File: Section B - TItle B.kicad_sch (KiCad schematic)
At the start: 0 parts

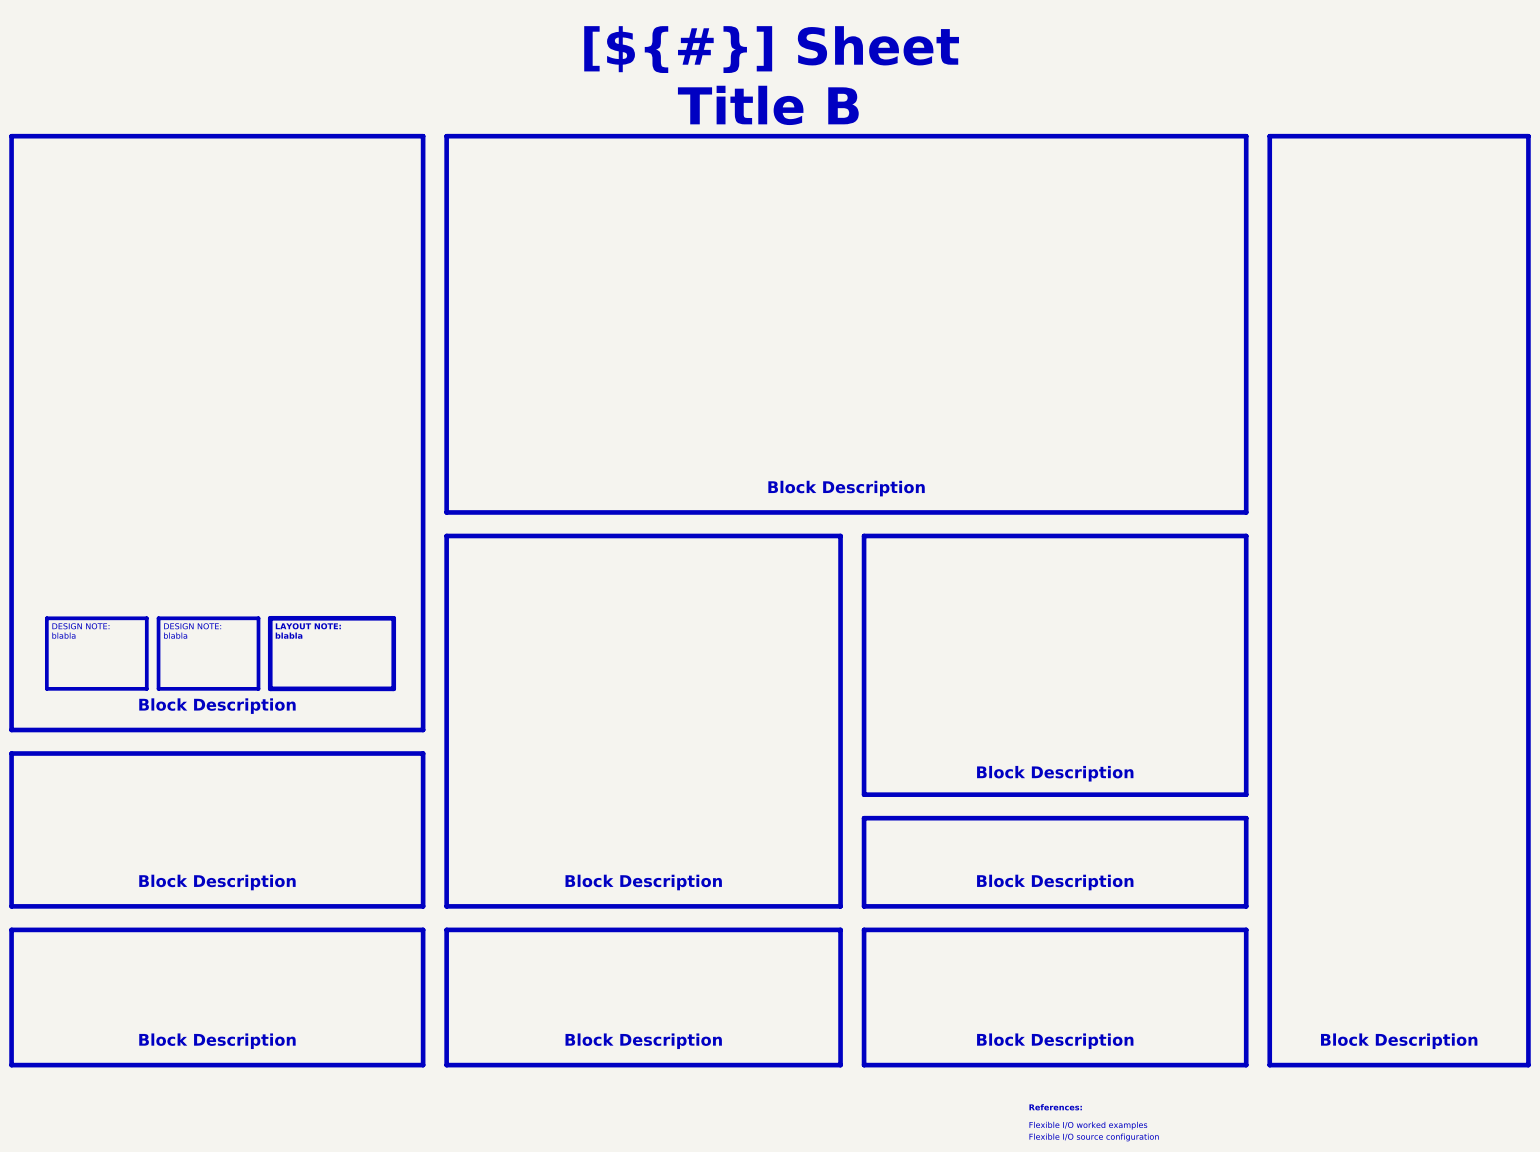
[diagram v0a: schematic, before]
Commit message: [added] completed initial sch design, move from draft to preliminary
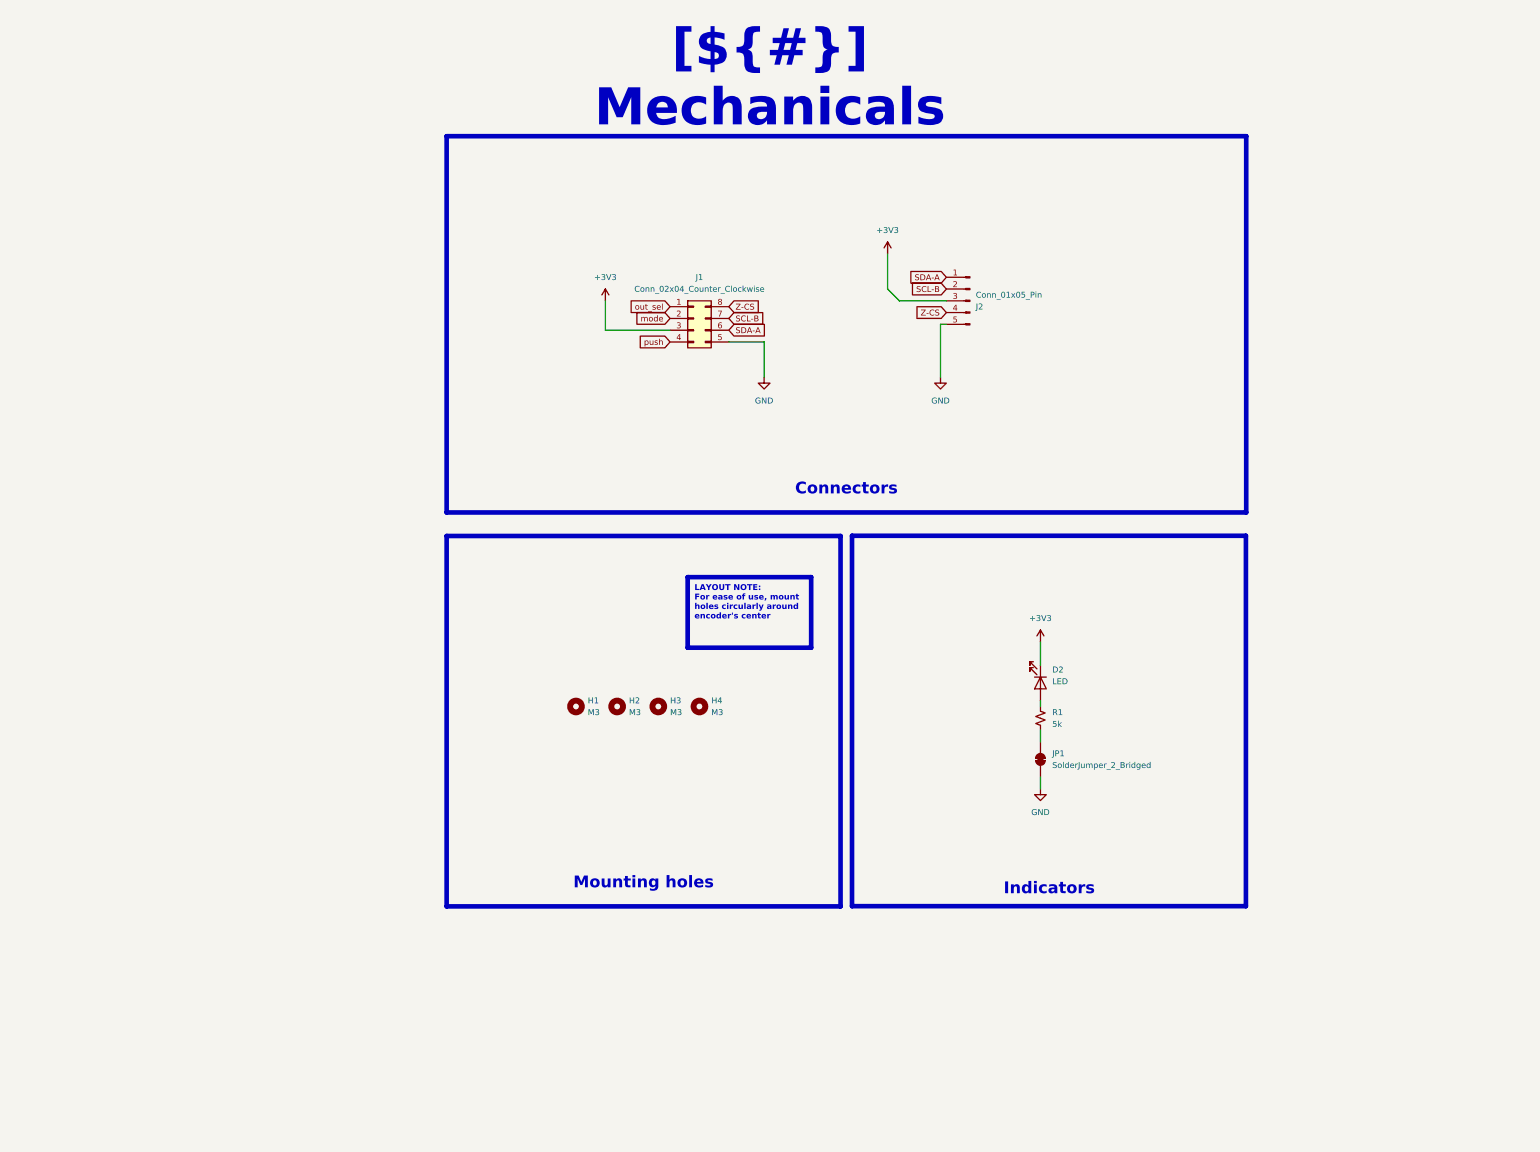
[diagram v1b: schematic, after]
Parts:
- added D2: LED, LED_SMD:LED_0603_1608Metric, symbol Device:LED
- added H1, H2, H3, H4: M3, MountingHole:MountingHole_3.2mm_M3, symbol Mechanical:MountingHole
- added J1: Conn_02x04_Counter_Clockwise, Connector_PinHeader_2.54mm:PinHeader_2x06_P2.54mm_Vertical, symbol Connector_Generic:Conn_02x04_Counter_Clockwise
- added J2: Conn_01x05_Pin, Connector_JST:JST_SH_BM05B-SRSS-TB_1x05-1MP_P1.00mm_Vertical, symbol Connector:Conn_01x05_Pin
- added JP1: SolderJumper_2_Bridged, Jumper:SolderJumper-2_P1.3mm_Bridged_RoundedPad1.0x1.5mm, symbol Jumper:SolderJumper_2_Bridged
- added R1: 5k, Resistor_SMD:R_0402_1005Metric, symbol Device:R_Small_US
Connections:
- new net: D2.2 (A), R1.1
- new net: JP1.2 (B), R1.2
- new net +3V3: D2.1 (K), J1.3 (Pin_3), J2.3 (Pin_3)
- new net GND: J1.5 (Pin_5), J2.5 (Pin_5), JP1.1 (A)
- new net SCL-B: J1.7 (Pin_7), J2.2 (Pin_2)
- new net SDA-A: J1.6 (Pin_6), J2.1 (Pin_1)
- new net Z-CS: J1.8 (Pin_8), J2.4 (Pin_4)
- new net mode: J1.2 (Pin_2)
- new net out_sel: J1.1 (Pin_1)
- new net push: J1.4 (Pin_4)
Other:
- note removed: "Flexible I/O source configuration"
- note removed: "Flexible I/O worked examples"
- note removed: "References:"
- title: Sheet Title B -> Mechanicals
